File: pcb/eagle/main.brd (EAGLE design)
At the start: 50 x 50 mm, 10 parts

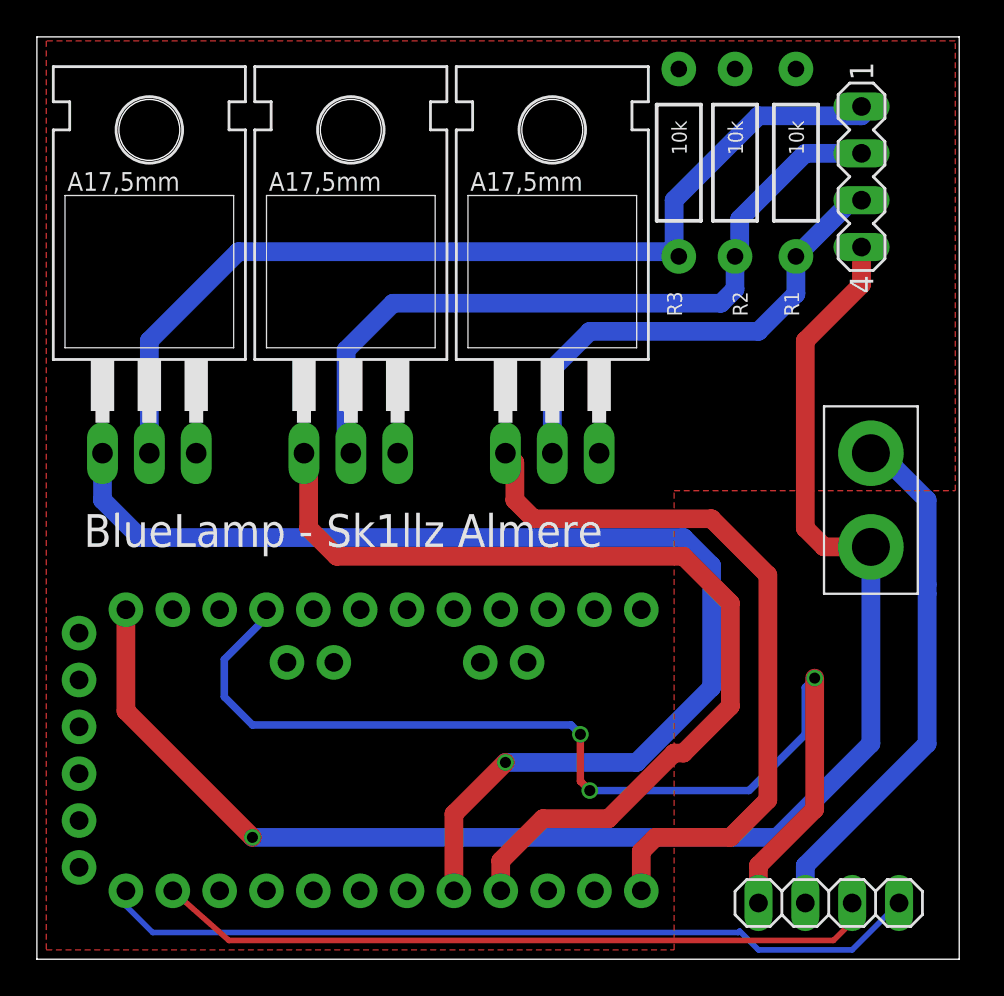
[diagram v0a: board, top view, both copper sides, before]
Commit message: Update PCB design to single-sided
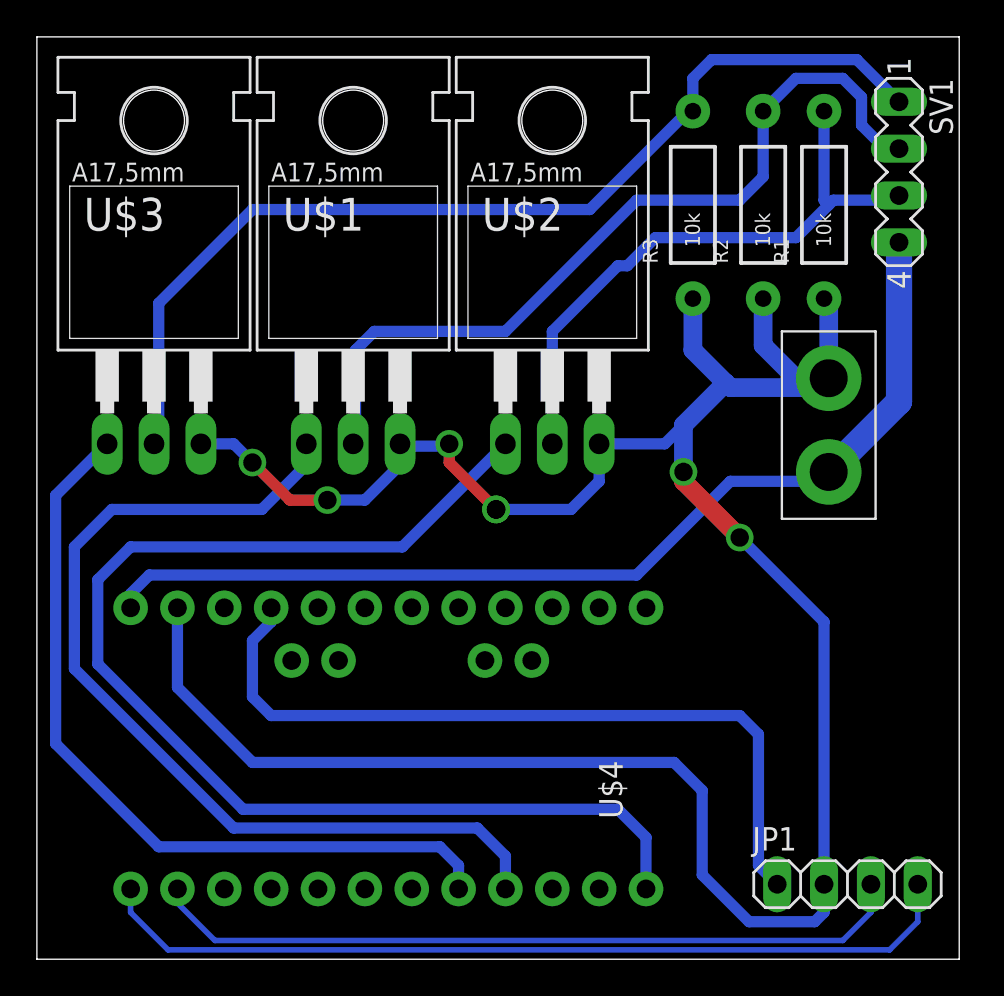
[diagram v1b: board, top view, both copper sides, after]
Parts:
- moved JP2 4.66 mm to (42.9, 29.0)
- moved R2 2.75 mm to (39.4, 40.9), turned to 90 degrees
- moved R1 2.75 mm to (42.7, 40.9), turned to 90 degrees
- moved R3 2.41 mm to (35.6, 40.9), turned to 90 degrees
- moved SV1 2.05 mm to (46.7, 42.7)
- moved JP1 1.44 mm to (43.9, 4.06)
- moved U$3 0.57 mm to (6.35, 34.3)
- moved U$1 0.52 mm to (17.1, 34.3)
- moved U$2 0.51 mm to (27.9, 34.3)
- moved U$4 0.27 mm to (17.8, 11.4)
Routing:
- net GND: track 28.7 -> 137.3 mm, vias 0 -> 6
- net N$5: track 82.0 -> 55.4 mm, vias 1 -> 0
- net N$4: track 40.5 -> 66.1 mm
- net N$2: track 64.6 -> 43.3 mm, vias 1 -> 0
- net VCC: track 58.7 -> 42.1 mm, vias 3 -> 0
- net N$8: track 26.3 -> 33.1 mm
- net N$9: track 40.1 -> 45.3 mm
- net N$6: track 53.0 -> 55.7 mm
- net RX: track 44.9 -> 47.4 mm
- net TX: track 39.3 -> 41.4 mm
- removed copper zone on layer 1, net GND
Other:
- board text removed: "BlueLamp - Sk1llz Almere"

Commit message: Update PCB to fix pulldown resistor problem
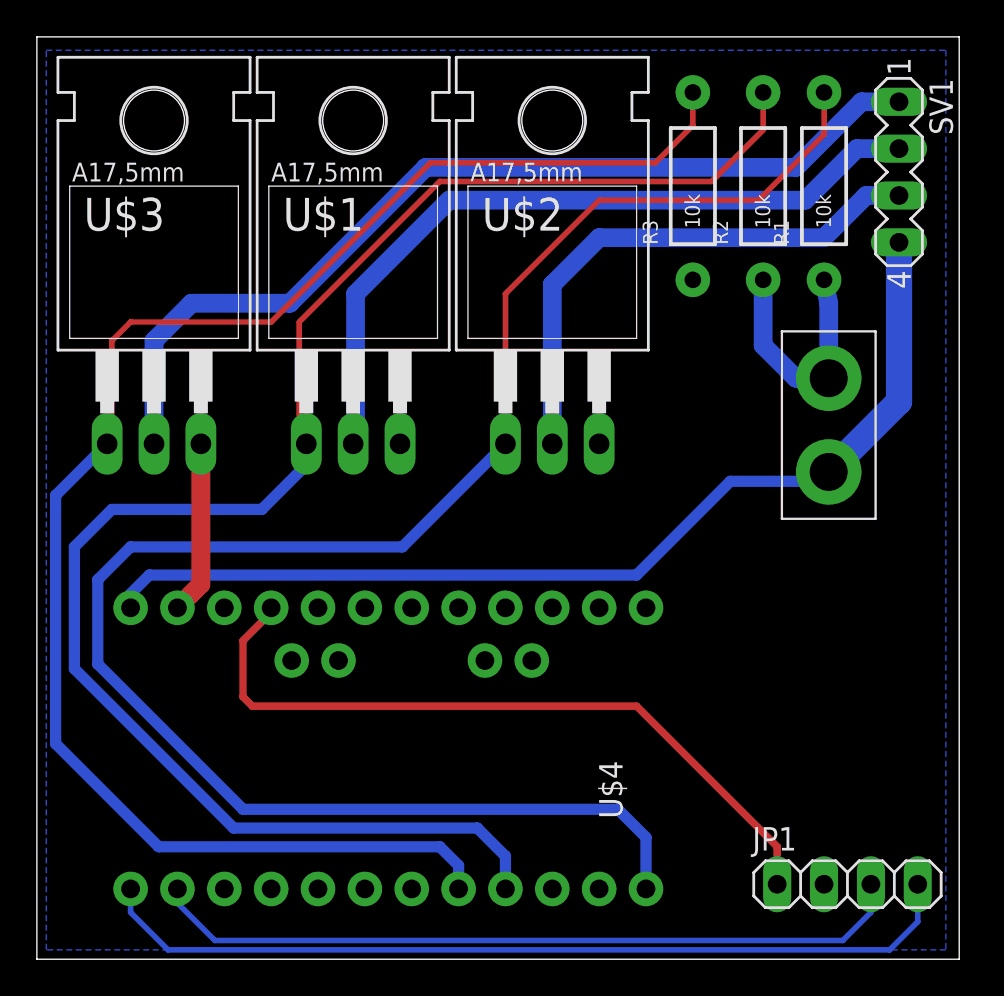
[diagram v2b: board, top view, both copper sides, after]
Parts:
- moved R1 1.02 mm to (42.7, 41.9)
- moved R2 1.02 mm to (39.4, 41.9)
- moved R3 1.02 mm to (35.6, 41.9)
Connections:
- net N$2: now also R3.P$2
- net N$3: now also R2.P$2
- net N$4: now also R1.P$2
- net N$6: no longer R3.P$2
- net N$8: no longer R1.P$2
- net N$9: no longer R2.P$2
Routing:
- net GND: track 137.3 -> 22.6 mm, vias 6 -> 0
- net N$2: track 43.3 -> 87.1 mm
- net N$3: track 51.5 -> 89.8 mm
- net N$4: track 66.1 -> 97.4 mm
- net N$9: track 45.3 -> 40.9 mm
- net N$6: track 55.7 -> 51.3 mm
- net N$8: track 33.1 -> 29.4 mm
- net VCC: track 42.1 -> 39.8 mm
- added copper zone on layer 16, net GND
